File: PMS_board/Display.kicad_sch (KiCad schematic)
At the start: 5 parts, among them Q1 BSS138

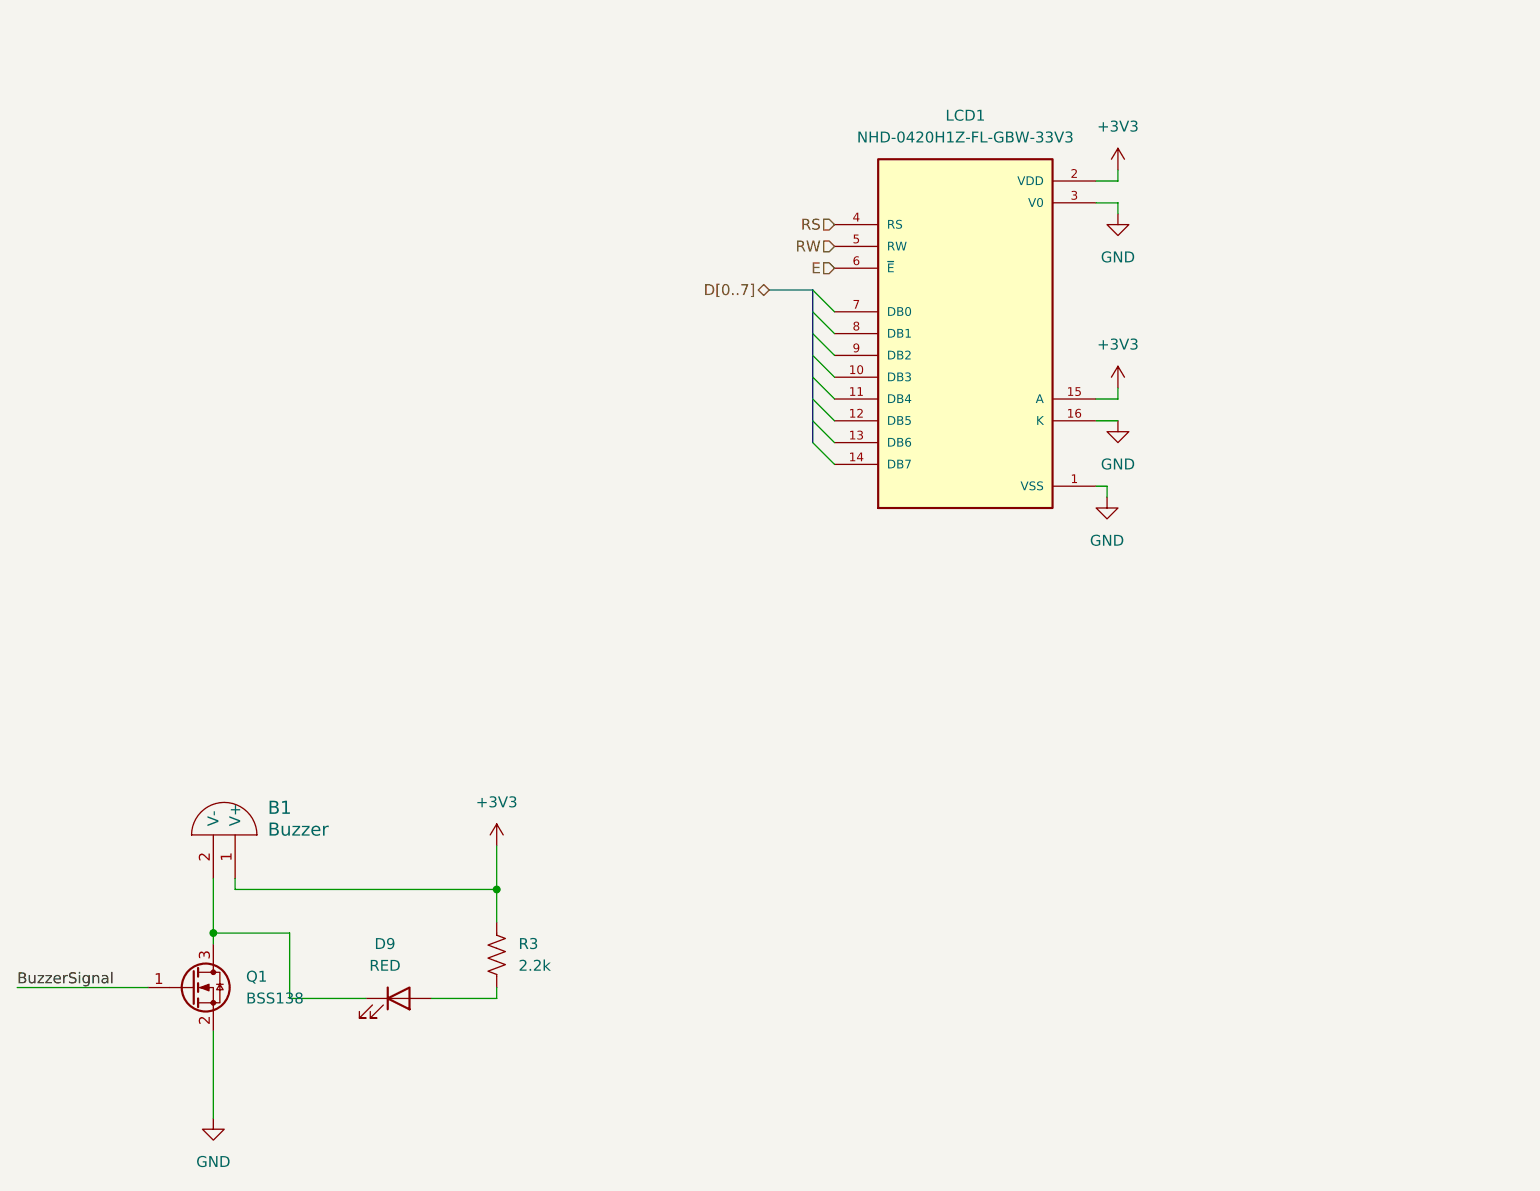
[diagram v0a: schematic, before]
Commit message: add converter and friends
I added the converter symbols and updated the schematic. I chose the proper FETs and Diodes for ORing circuit.
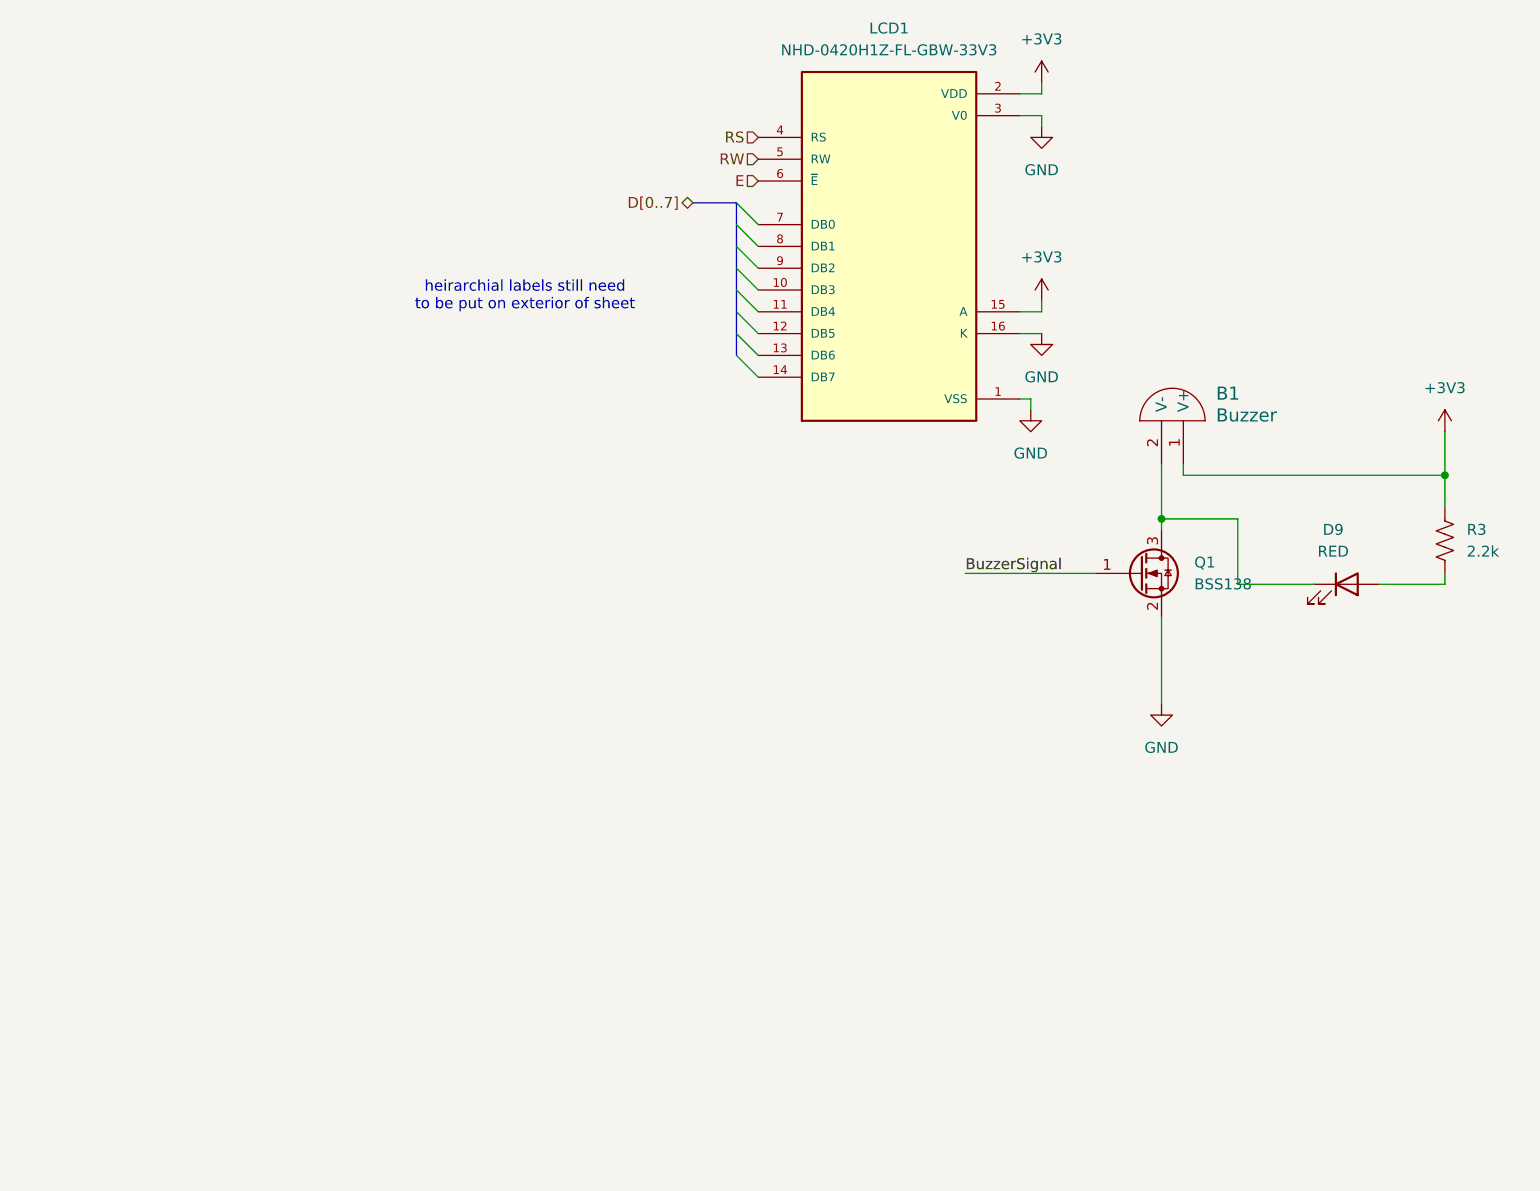
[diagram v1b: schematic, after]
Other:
- note added: "heirarchial labels still need to be put on exterior of sheet"
- moved on the sheet: B1, D9, LCD1, Q1, R3

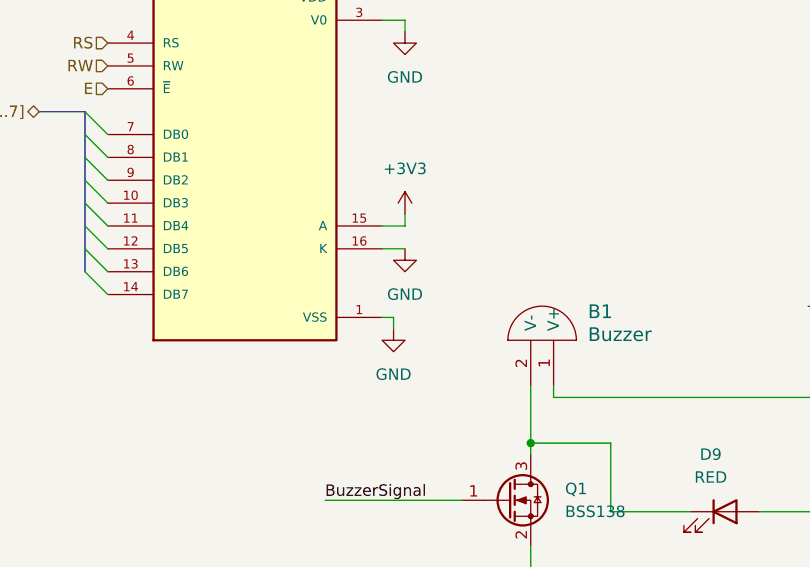
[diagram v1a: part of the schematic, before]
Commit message: Add Bucks & Fix Issues
- Added 3V3 and 5V buck convertors
- Removed Pi filter
- adjusted capacitor values for Bulk Capacitors
- Added inrush protection to ORing circuit
- renamed various hierarchical pins for clarity
- renamed power rail pins due to naming conflicts
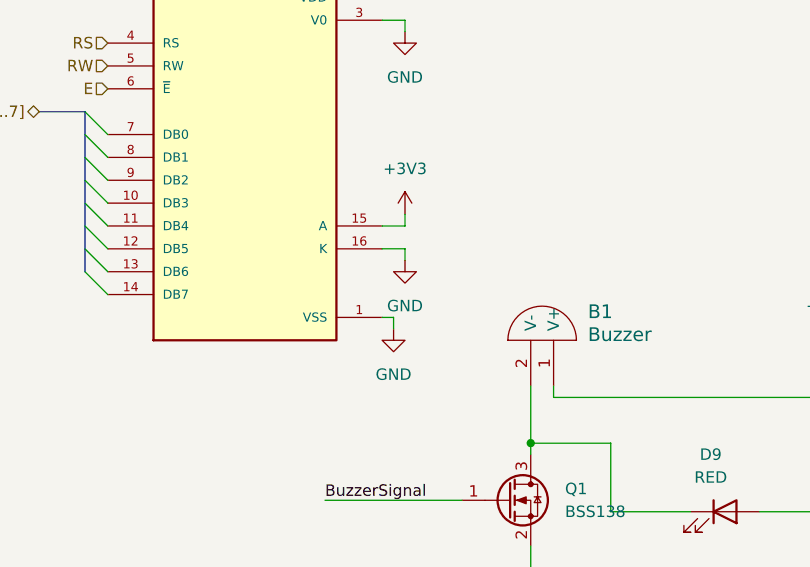
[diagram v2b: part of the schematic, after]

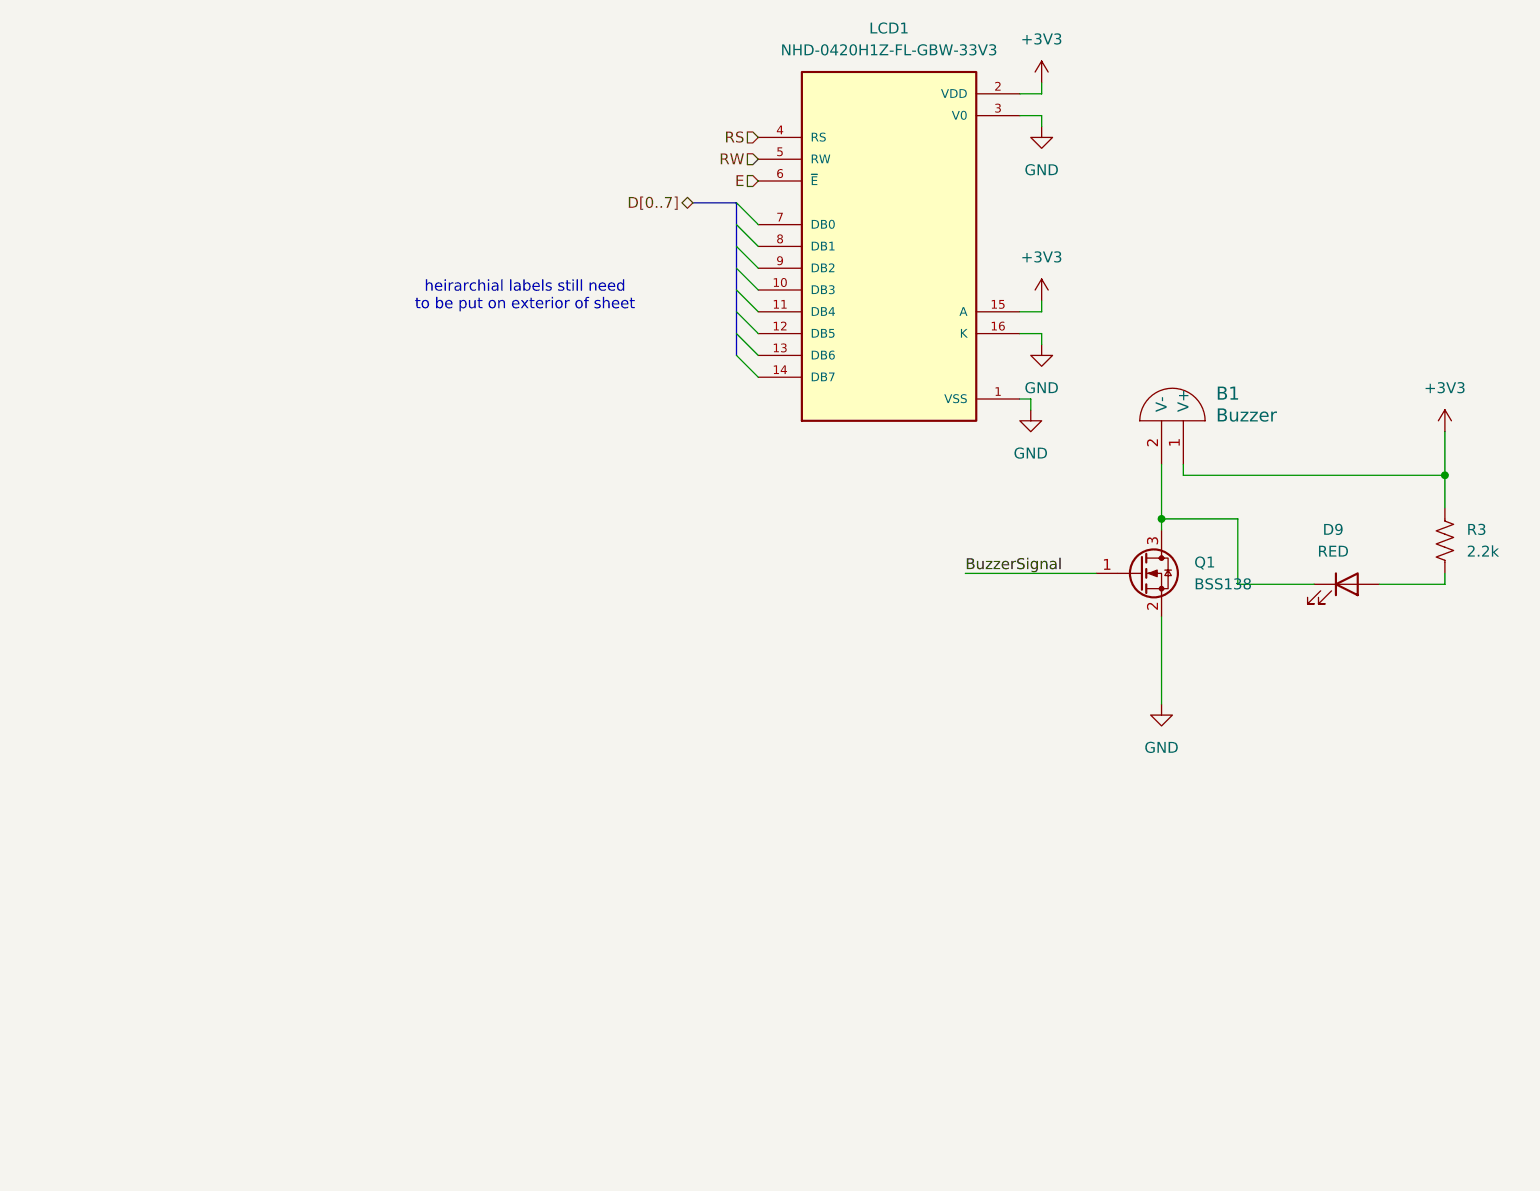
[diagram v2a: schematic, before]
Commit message: Refine Current Sensing
- Removed redundant current sensors
- Fixed hierarchical labelling for sensors
- added labeling for a few circuits
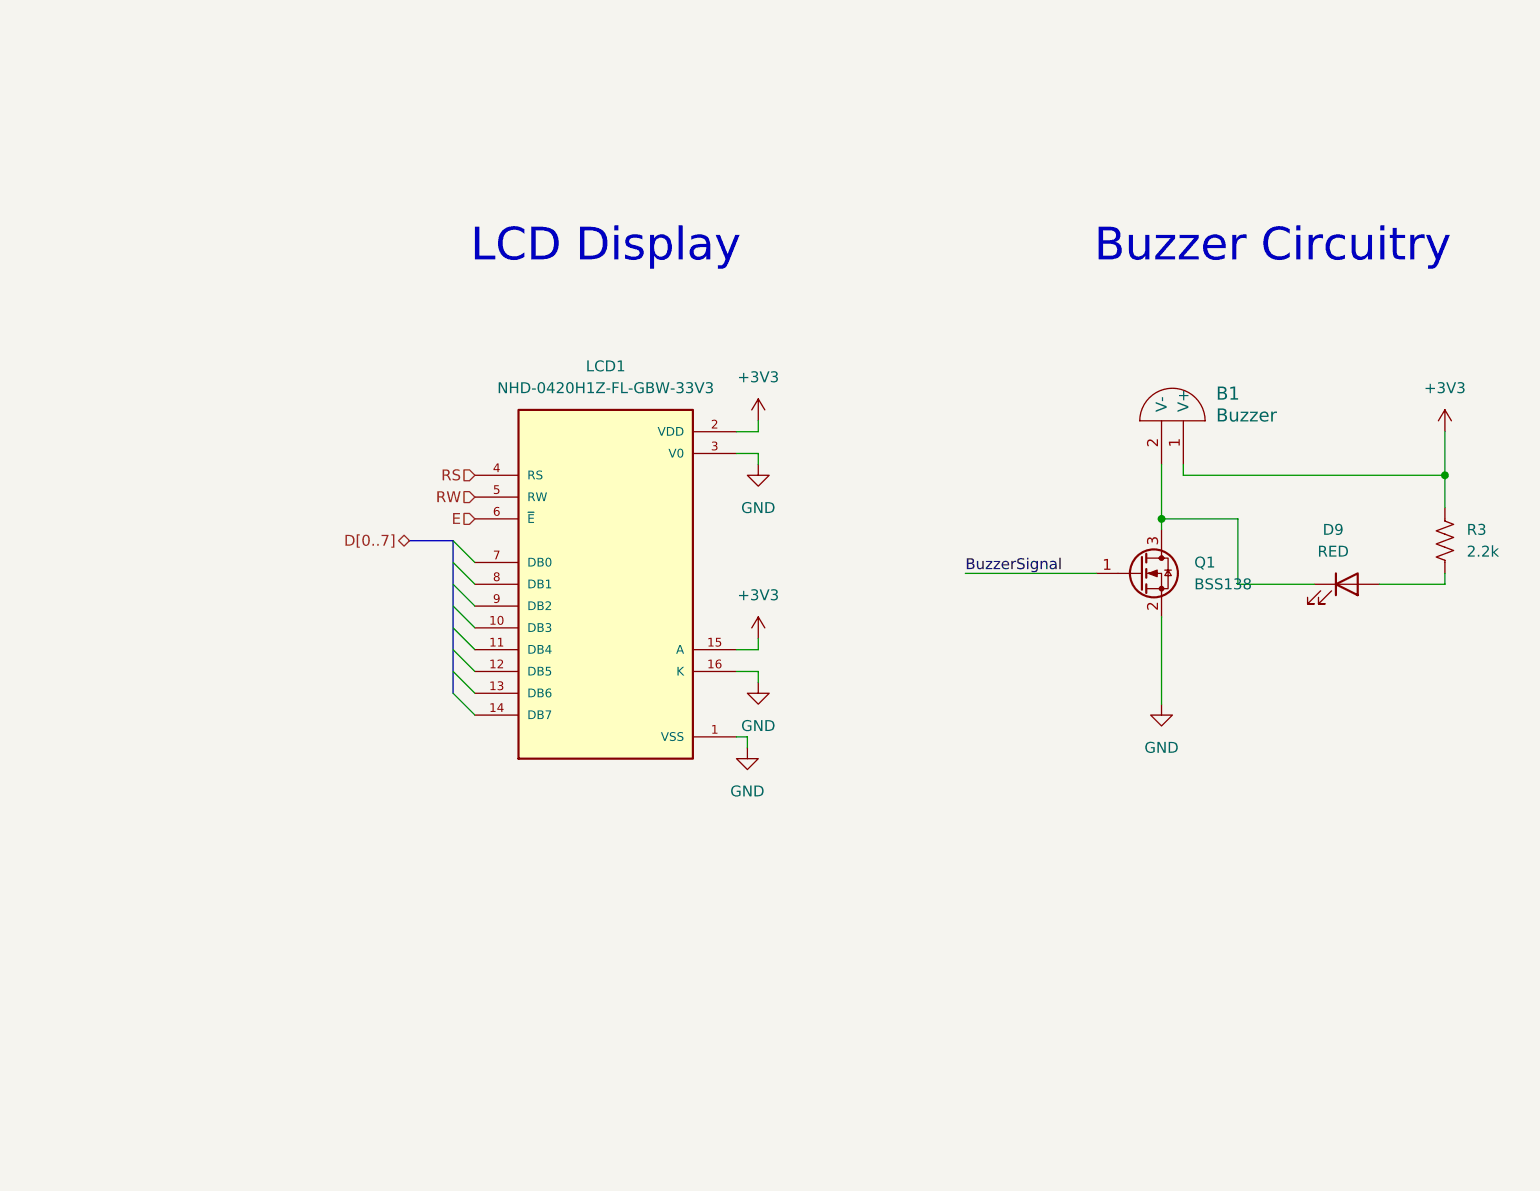
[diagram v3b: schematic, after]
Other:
- note added: "Buzzer Circuitry"
- note added: "LCD Display"
- note removed: "heirarchial labels still need to be put on exterior of sheet"
- moved on the sheet: LCD1
